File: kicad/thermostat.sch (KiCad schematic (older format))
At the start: 59 parts, among them IC1 LM2596S-5, J1 Display i2c, J31 Conn_02x03_Odd_Even, J6 Screw_Terminal_01x05, T1 SIR424DP, U11 LTC4041, U21 BMP280

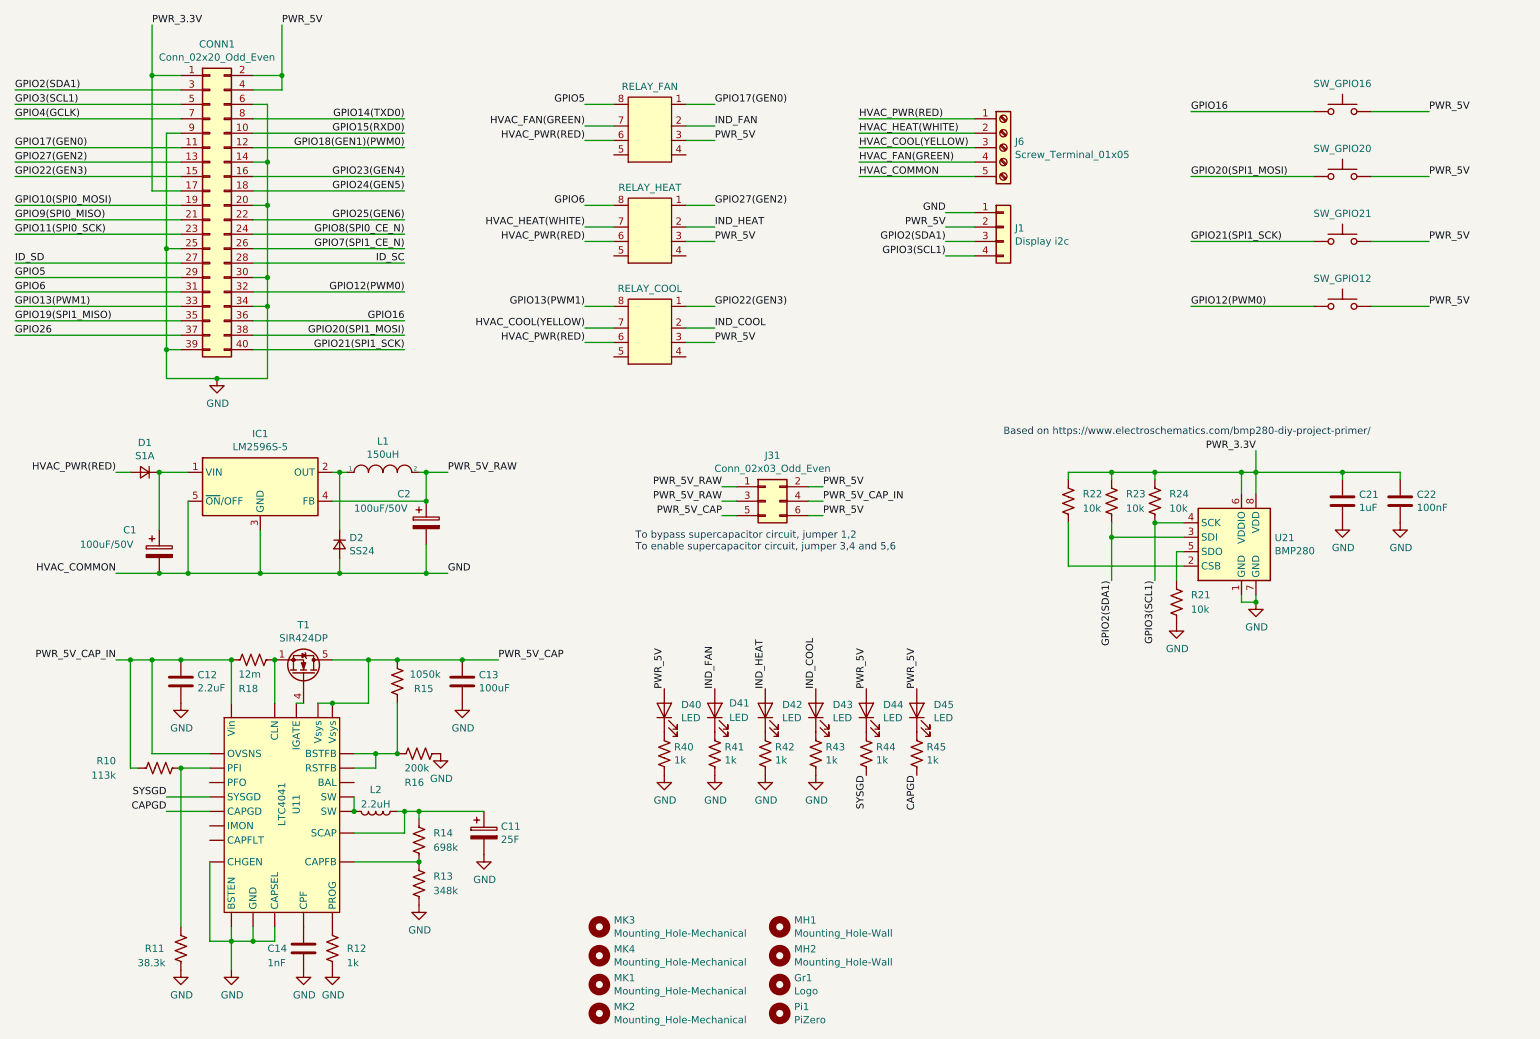
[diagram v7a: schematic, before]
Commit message: ltc4041 overall design ready
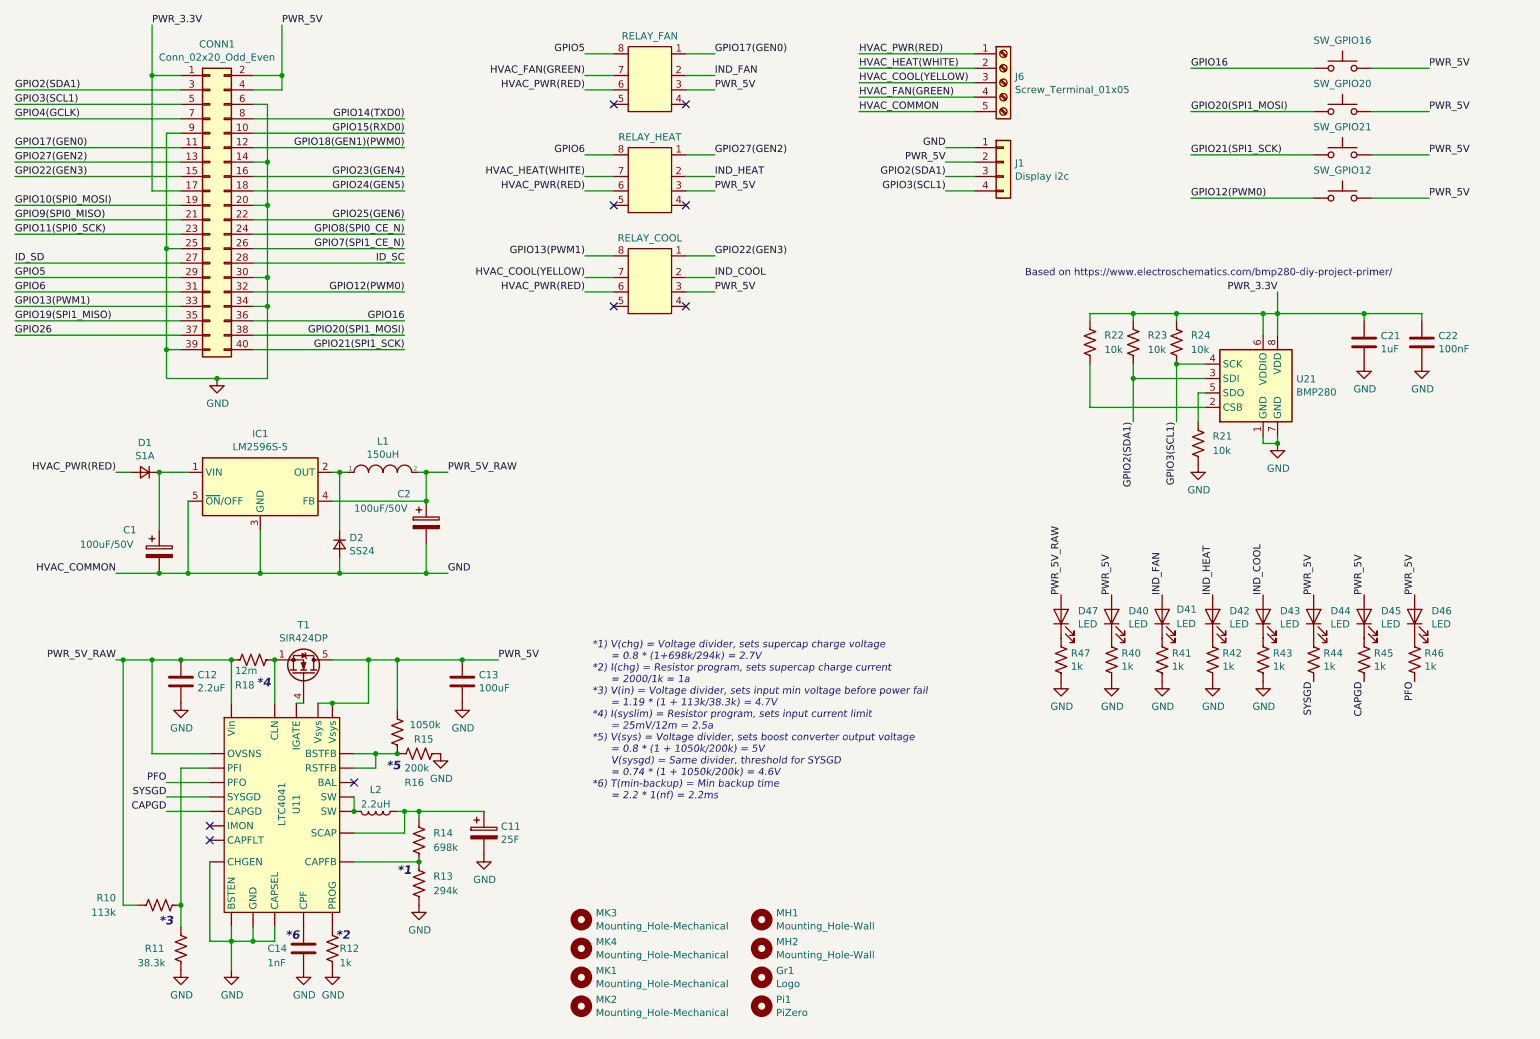
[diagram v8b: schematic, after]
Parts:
- removed J31: Conn_02x03_Odd_Even, Connector_PinHeader_2.54mm:PinHeader_2x03_P2.54mm_Vertical, symbol Connector_Generic:Conn_02x03_Odd_Even
- added D46, D47: LED, LED_SMD:LED_0805_2012Metric, symbol Device:LED
- added R46, R47: 1k, Resistor_SMD:R_0805_2012Metric, symbol Device:R_US
- C11: footprint Capacitor_THT:C_Radial_D16.0mm_H31.5mm_P7.50mm -> Capacitor_THT:CP_Radial_D18.0mm_P7.50mm; Mouser 504-HB1625-2R5256-R -> 594-MAL222591004E3
- R13: value 348k -> 294k
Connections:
- net PWR_5V_CAP is gone; now on net PWR_5V: C13.1, R15.2, T1.5 (D), U11.1 (Vsys), U11.24 (Vsys)
- net PWR_5V_CAP_IN is gone; now on net PWR_5V_RAW: C12.1, R10.1, R18.2, U11.16 (OVSNS), U11.6 (Vin)
- net GND: now also R47.2
- net PWR_5V: now also D46.2 (A)
- net PWR_5V_RAW: now also D47.2 (A)
- net PFO: now reaches U11.14 (PFO)
- net PFO: now also R46.2
- new net: D46.1 (K), R46.1
- new net: D47.1 (K), R47.1
- no-connect marks 0 -> 9
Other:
- note added: "*1"
- note added: "*1) V(chg) = Voltage divider, sets supercap charge voltage\n = 0.8 * (1+698k/294k) = 2.7V\n*2) I(chg) = Resistor program, sets supercap charge current\n = 2000/1k = 1a\n*3) V(in) = Voltage divider, sets input min voltage before power fail\n = 1.19 * (1 + 113k/38.3k) = 4.7V\n*4) I(syslim) = Resistor program, sets input current limit\n = 25mV/12m = 2.5a\n*5) V(sys) = Voltage divider, sets boost con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"
- note added: "*2"
- note added: "*3"
- note added: "*4"
- note added: "*5"
- note added: "*6"
- note removed: "To bypass supercapacitor circuit, jumper 1,2\nTo enable supercapacitor circuit, jumper 3,4 and 5,6"
- moved on the sheet: C21, C22, D40, D41, D42, D43, D44, D45, Gr1, J1, J6, MH1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
